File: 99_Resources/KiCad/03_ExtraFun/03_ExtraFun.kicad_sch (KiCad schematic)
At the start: 6 parts

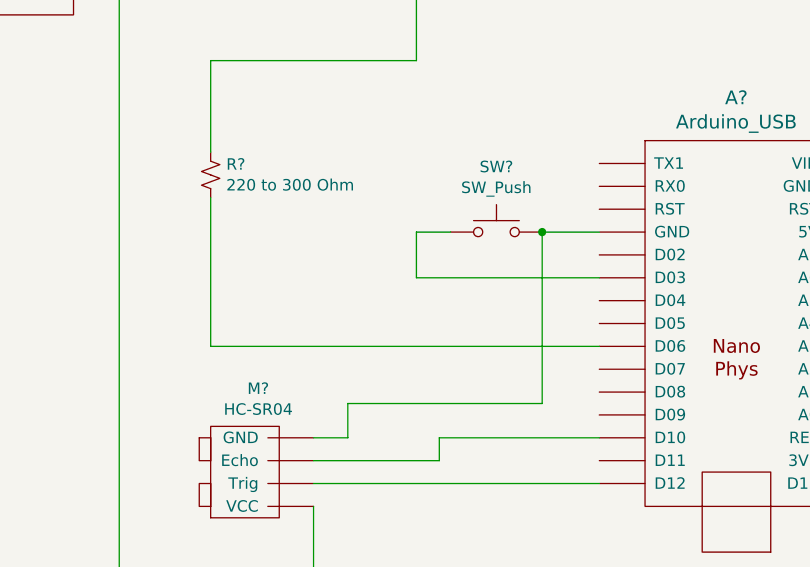
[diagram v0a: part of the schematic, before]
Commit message: make pin numbers consistent, more DemoReelSound work
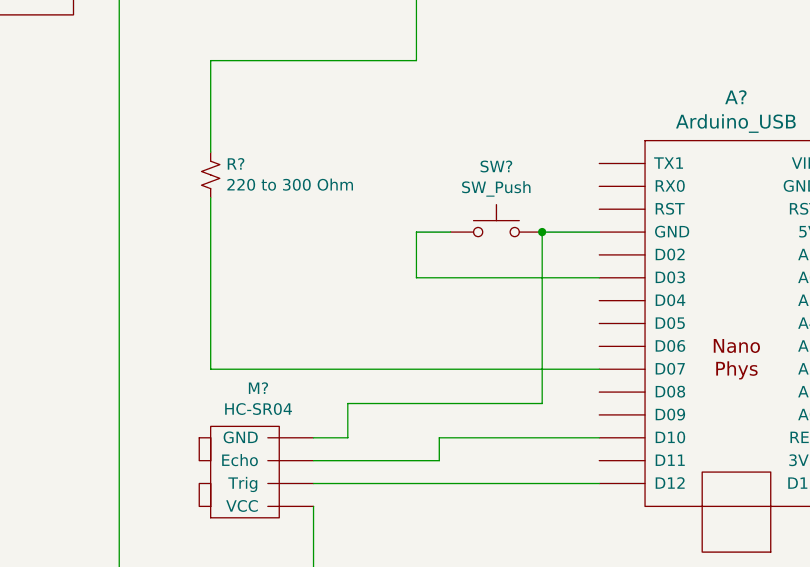
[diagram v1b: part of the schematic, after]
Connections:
- net at A?.~ (VIN): now also Z?.~ (GND)
- net at Z?.~ (GND): no longer A?.~ (VIN)
- new net: A?.~ (VIN), M?.~ (VCC), SW?.2
- new net: A?.~ (VIN), M?.~ (VCC) (x2)
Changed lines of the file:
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@@
+    (stroke (width 0) (type default))
+  )
+  (wire (pts (xy 143.51 138.43) (xy 100.33 138.43))
     (stroke (width 0) (type default))
   )
@@
     (stroke (width 0) (type default))
   )
-  (wire (pts (xy 100.33 119.38) (xy 100.33 135.89))
+  (wire (pts (xy 100.33 119.38) (xy 100.33 138.43))
     (stroke (width 0) (type default))
   )
@@
     (stroke (width 0) (type default))
   )
-  (wire (pts (xy 100.33 135.89) (xy 143.51 135.89))
-    (stroke (width 0) (type default))
-  )
